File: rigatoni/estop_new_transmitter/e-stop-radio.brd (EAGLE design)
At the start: 160 x 100 mm, 71 parts, among them J2 AVR_SPI_PROG_3X2PTH, J3 UX60-MB-5S8, J4 5-1814832-1, Q1 MMUN2133LT1G, U1 ATMEGA32U4-AU, U2 MCP73831T-2ACI/OT, U3 TPS62203DBVR, U4 TPS61090RSAR, U5 RFM69HCW, U6 SN74ALVC164245DGGR, X1 TSX-3225 16.0000MF18X-AC0

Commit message: Rough PCB Design Complete
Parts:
- moved R7 200.0 mm to (130.8, 66.0), turned to 180 degrees
- moved C21 192.9 mm to (129.5, 40.6), turned to 270 degrees
- moved F2 192.3 mm to (123.2, 49.5), turned to 90 degrees
- moved C19 177.9 mm to (127.0, 40.6), turned to 270 degrees
- moved C10 166.4 mm to (100.3, 52.1), flipped to the bottom, turned to 180 degrees
- moved C18 165.8 mm to (123.2, 55.9), turned to 90 degrees
- moved R26 164.7 mm to (127.0, 44.5)
- moved R24 161.7 mm to (130.8, 63.5), turned to 180 degrees
- moved R25 159.2 mm to (119.4, 44.5)
- moved R23 155.1 mm to (127.0, 63.5), turned to 180 degrees
- moved C4 155.0 mm to (94.0, 61.0), flipped to the bottom, turned to 180 degrees
- moved R22 155.0 mm to (127.0, 40.6), flipped to the bottom
- moved F1 148.1 mm to (85.1, 50.8), flipped to the bottom, turned to 270 degrees
- moved C20 146.4 mm to (90.2, 49.5), turned to 270 degrees
- moved R16 142.6 mm to (123.2, 53.3), flipped to the bottom
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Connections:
- net BUTTN_1: now also J5.12; no longer J5.14
- net BUTTN_2: now also J5.11; no longer J5.13
- net BUTTN_3: now also J5.10; no longer J5.12
- net BUTTN_4: now also J5.9; no longer J5.11
- net DIO_4_R: now also J5.8; no longer J5.10
- net DIO_5_R: now also J5.7; no longer J5.9
- net DIO_6_R: now also J5.6; no longer J5.8
- net DIO_7_R: now also J5.5; no longer J5.7
- net DIO_7_R1: now also J5.4; no longer J5.6
- net DIO_7_R2: now also J5.3; no longer J5.5
- net DIO_7_R3: now also J5.13; no longer J5.4
- net ENABLE: now also J5.14; no longer J5.2
- net H4: now also J5.2; no longer J5.3

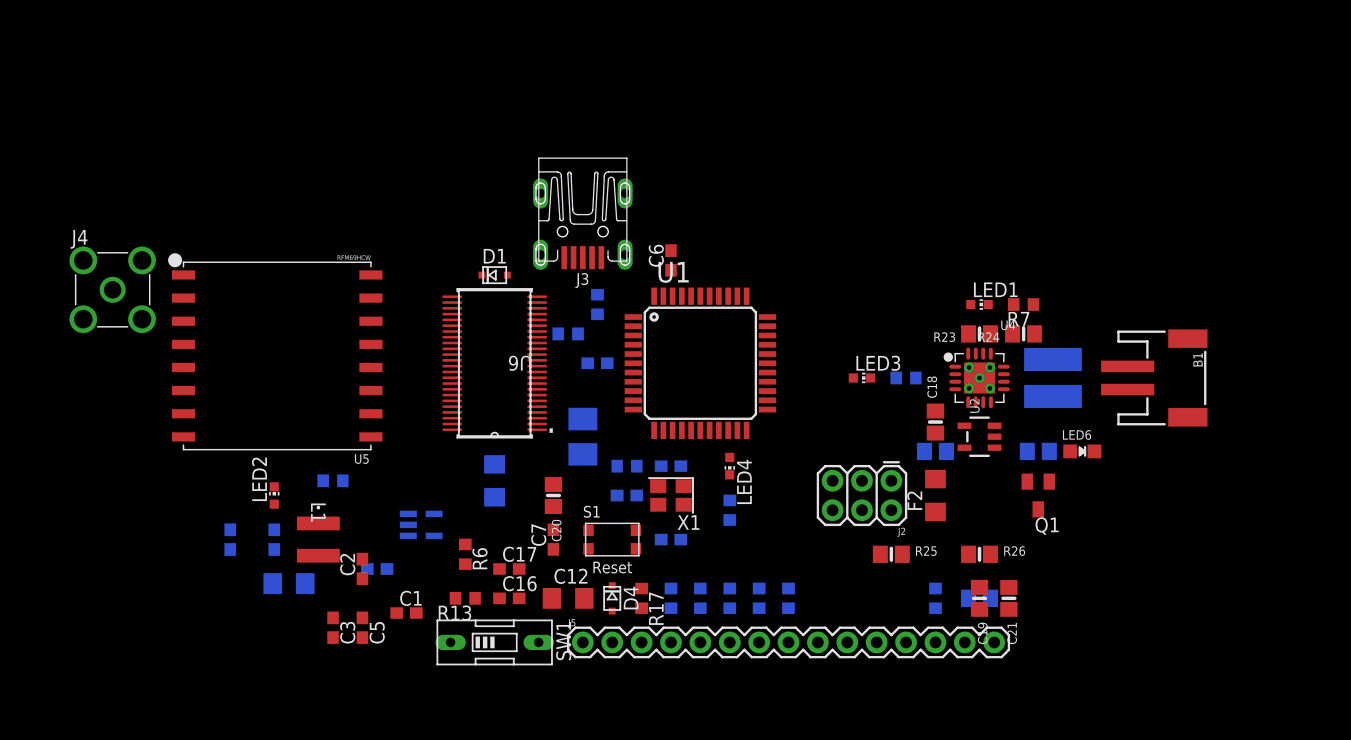
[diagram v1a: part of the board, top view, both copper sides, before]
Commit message: eStopV2 Rough Draft Complete
Optimization is still needed
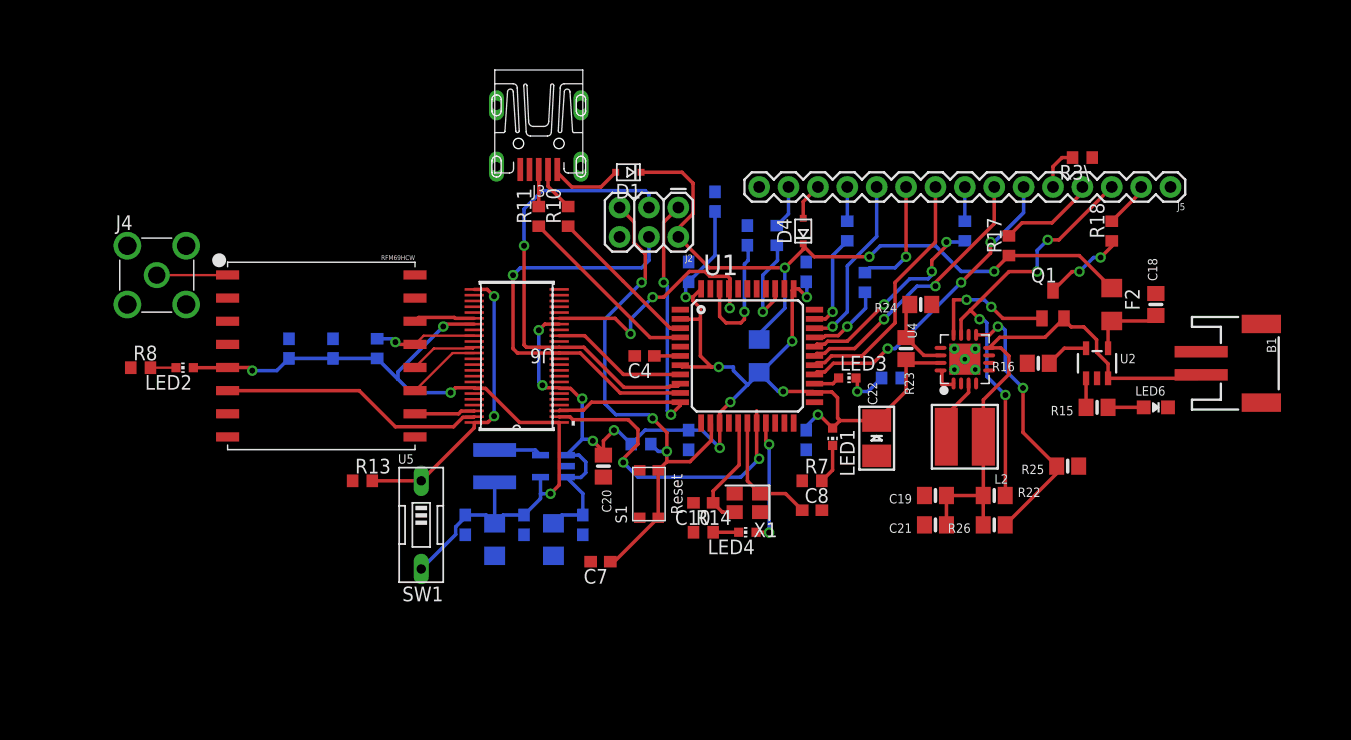
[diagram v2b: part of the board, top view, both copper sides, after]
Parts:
- moved J5 64.3 mm to (143.5, 76.2), turned to 180 degrees
- moved R3\ 48.8 mm to (135.9, 78.7), flipped to the top, turned to 180 degrees
- moved C1 45.4 mm to (112.0, 68.9), flipped to the bottom, turned to 90 degrees
- moved R17 44.0 mm to (129.5, 71.1), turned to 90 degrees
- moved C13 43.1 mm to (104.1, 74.9), turned to 90 degrees
- moved C5 41.7 mm to (101.9, 68.9), flipped to the bottom, turned to 90 degrees
- moved C2 39.9 mm to (112.0, 54.3), flipped to the bottom, turned to 270 degrees
- moved D4 35.8 mm to (111.8, 72.4), turned to 90 degrees
- moved R18 35.2 mm to (138.4, 72.4), flipped to the top, turned to 90 degrees
- moved R5 35.2 mm to (125.7, 72.4), turned to 90 degrees
- moved C3 34.8 mm to (101.9, 54.3), flipped to the bottom
- moved R2 34.2 mm to (115.6, 72.4), turned to 90 degrees
- moved R12 32.7 mm to (109.5, 72.0), turned to 90 degrees
- moved J2 30.0 mm to (101.0, 74.4)
- moved R4 28.8 mm to (117.1, 67.9), turned to 90 degrees
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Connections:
- net BUTTN_1: now also J5.6; no longer J5.12
- net BUTTN_2: now also J5.9; no longer J5.11
- net BUTTN_3: now also J5.7; no longer J5.10
- net BUTTN_4: now also J5.11; no longer J5.9
- net DIO_5_R: now also J5.10; no longer J5.7
- net DIO_6_R: now also J5.5; no longer J5.6
- net DIO_7_R: now also J5.12; no longer J5.5
- net DIO_7_R1: now also J5.14; no longer J5.4
- net DIO_7_R2: now also J5.4; no longer J5.3
- net DIO_7_R3: now also J5.2; no longer J5.13
- net ENABLE: now also J5.3; no longer J5.14
- net H4: now also J5.13; no longer J5.2
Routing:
- net 5V: track 0.00 -> 117.5 mm, vias 0 -> 13
- net +3.3V: track 0.00 -> 70.5 mm, vias 0 -> 4
- net 5V_UNFUSED: track 0.00 -> 60.4 mm, vias 0 -> 3
- net MCU_RST: track 0.00 -> 46.9 mm, vias 0 -> 3
- net VBAT: track 0.00 -> 46.3 mm
- net SCK_5V: track 0.00 -> 39.6 mm, vias 0 -> 1
- net ENABLE: track 0.00 -> 37.6 mm, vias 0 -> 4
- net MOSI_5V: track 0.00 -> 36.7 mm, vias 0 -> 1
- net MISO_5V: track 0.00 -> 30.9 mm, vias 0 -> 2
- net DATA_AVAILABLE_5V: track 0.00 -> 27.8 mm, vias 0 -> 2
- net BUTTN_1: track 0.00 -> 26.6 mm, vias 0 -> 3
- net SHIFTER_EN: track 0.00 -> 25.4 mm, vias 0 -> 2
- net BUTTN_3: track 0.00 -> 23.6 mm, vias 0 -> 2
- net N$14: track 0.00 -> 23.5 mm, vias 0 -> 2
- net DATA_AVAILABLE_3V: track 0.00 -> 23.0 mm
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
